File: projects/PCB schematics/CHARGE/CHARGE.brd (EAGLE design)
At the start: 160 x 100 mm, 42 parts, among them IC2 78L08SMD, Q1 IRLZ44Z, Q2 IRLZ44Z, Q3 IRLZ44Z, Q4 IRLZ44Z

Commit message: TSMPC - Initial draft (WIP).
Non-working commit of TSMPC.
Done simply to show possible board layout.
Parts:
- moved C9 435.3 mm to (96.5, 38.1)
- moved C11 431.1 mm to (106.7, 25.4)
- moved C10 430.7 mm to (99.1, 25.4)
- moved C8 430.4 mm to (91.4, 25.4)
- moved R10 428.1 mm to (82.5, 10.2)
- moved C7 426.7 mm to (106.7, 30.5)
- moved AND1 419.9 mm to (49.5, 3.81), turned to 90 degrees
- moved R14 417.9 mm to (64.8, 5.08), turned to 270 degrees
- moved OK1 415.6 mm to (74.9, 7.62), turned to 270 degrees
- moved C6 402.9 mm to (102.9, 11.4), turned to 90 degrees
- moved IC2 396.3 mm to (90.2, 16.5), turned to 90 degrees
- moved HV-OPA 375.6 mm to (90.2, 7.62), turned to 90 degrees
- moved R11 335.4 mm to (61.0, 17.8), turned to 90 degrees
- moved R13 324.7 mm to (58.4, 8.89)
- moved Q4 324.0 mm to (71.1, 27.9), turned to 270 degrees
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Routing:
- net AIR_CONTROL_SIGNAL: track 0.00 -> 109.9 mm, vias 0 -> 1
- net N$18: track 0.00 -> 99.0 mm, vias 0 -> 1
- net N$14: track 0.00 -> 88.2 mm
- net N$11: track 0.00 -> 84.9 mm
- net HV-: track 0.00 -> 81.7 mm
- net V+: track 0.00 -> 79.8 mm, vias 0 -> 2
- net N$24: track 0.00 -> 61.1 mm, vias 0 -> 1
- net HV+: track 0.00 -> 58.9 mm
- net VDIV_SIGNAL: track 0.00 -> 51.2 mm, vias 0 -> 2
- net +8V: track 0.00 -> 50.2 mm, vias 0 -> 4
- net HV-_CONTROL: track 0.00 -> 46.9 mm, vias 0 -> 1
- net N$9: track 0.00 -> 46.7 mm
- net N$3: track 0.00 -> 45.0 mm
- net N$7: track 0.00 -> 39.6 mm
- net VCC: track 0.00 -> 34.1 mm, vias 0 -> 2
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- added copper zone on layer 1, net GND
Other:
- board size 160 x 100 mm -> 111.7 x 86 mm

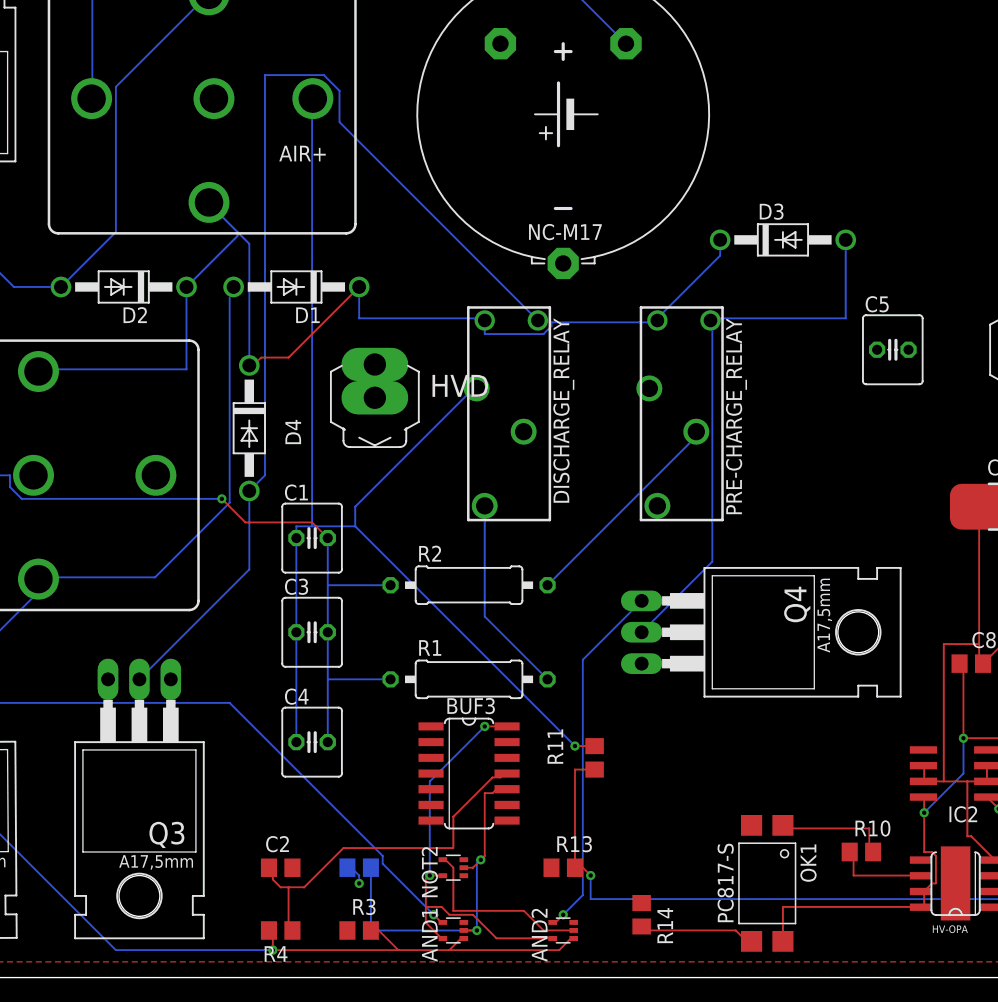
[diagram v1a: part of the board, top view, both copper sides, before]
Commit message: SC - Rev C; SC70 -> SOT23.
For single logic gate components, SC70 was initially chosen.
These packages proved too small to hand-solder.

All SC70 packages have been refactored to SOT23.

SparkFun DRC's added in for additional manufacturability.
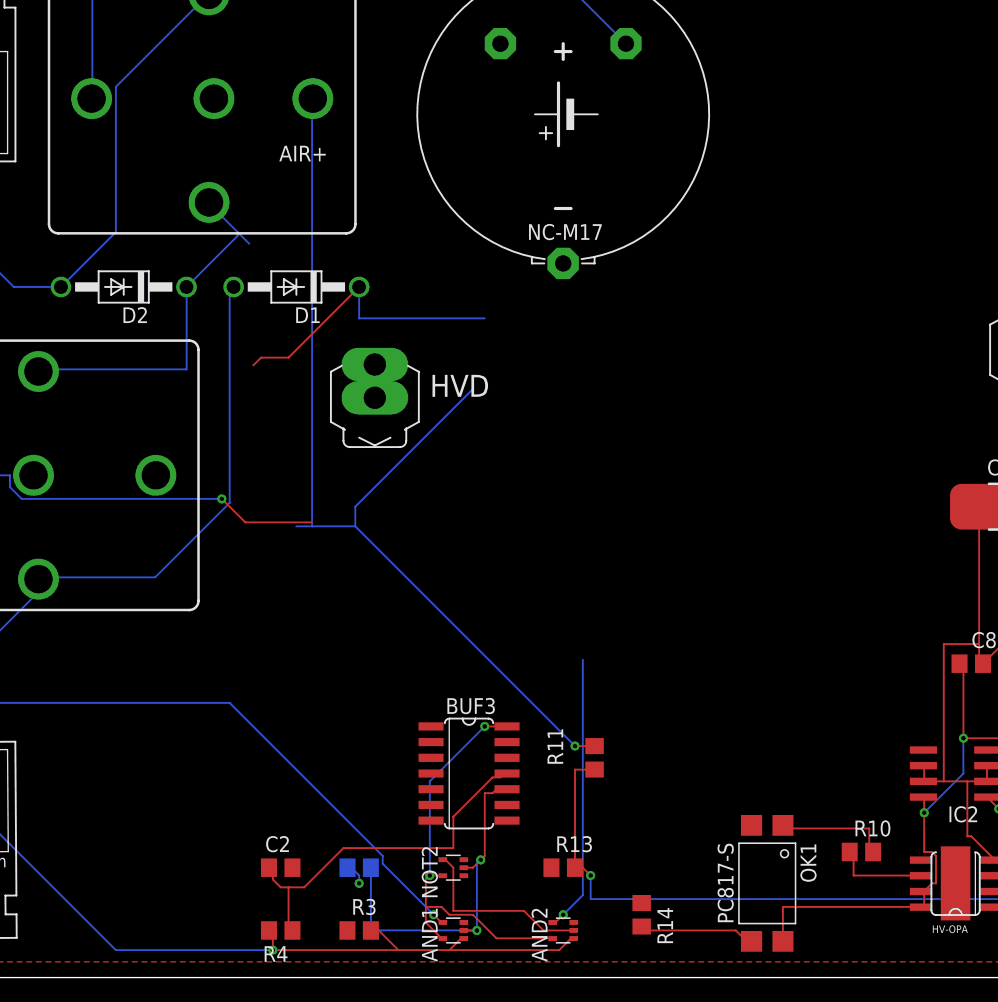
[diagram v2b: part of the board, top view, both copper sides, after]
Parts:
- removed C1, C3, C4, C5: (no value), rcl:C025-060X050
- removed D3, D4: 1N4933, diode:DO41-10
- removed DISCHARGE_RELAY, PRE-CHARGE_RELAY: CT112, relay:CT-SLIM
- removed Q3, Q4: IRLZ44Z, transistor-power:TO220BH
- removed R1, R2: (no value), rcl:0309/12
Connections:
- removed net N$1: PRE-CHARGE_RELAY.NO, R2.2
- removed net N$11: D4.A, DISCHARGE_RELAY.2, Q3.D
- removed net N$15: DISCHARGE_RELAY.NO
- removed net N$16: DISCHARGE_RELAY.C, R1.2
- removed net N$22: C5.2
- removed net N$23: C5.1
- removed net N$24: AIR-.87, C1.2, C3.2, C4.2, R1.1, R2.1
- removed net N$3: D3.A, PRE-CHARGE_RELAY.2, Q4.D
- removed net N$4: PRE-CHARGE_RELAY.NC
- new net N$27: AIR+.87
- new net N$31: AIR-.87
- net GND: no longer PRE-CHARGE_RELAY.C, Q3.S, Q4.S
- net N$14: no longer D3.C, D4.C, DISCHARGE_RELAY.1, PRE-CHARGE_RELAY.1
- net N$18: no longer AIR+.87, C1.1, C3.1, C4.1, DISCHARGE_RELAY.NC
- net N$2: no longer Q4.G
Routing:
- net N$11: track 84.9 -> 0.00 mm
- net N$24: track 61.1 -> 0.00 mm, vias 1 -> 0
- net N$3: track 45.0 -> 0.00 mm
- net N$14: track 88.2 -> 53.4 mm
- net N$31: track 0.00 -> 32.7 mm, vias 0 -> 1
- net N$18: track 99.0 -> 81.2 mm
- net N$1: track 17.5 -> 0.00 mm
- net N$16: track 16.1 -> 0.00 mm
- net N$2: track 29.1 -> 22.4 mm

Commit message: BSPD - Schematic revision/component revision.
During ESF, schematics chosen used European part libraries.
These were updated to US symbols, with appropriate final parts sourced
to allow builds of both SOP8 and DIL-8 packages.
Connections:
- new net N$1: HVD.1
- net N$14: no longer HVD.1
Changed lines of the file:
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@@
 </signal>
 <signal name="N$14">
-<contactref element="HVD" pad="1"/>
 <contactref element="AIR+" pad="86"/>
 <contactref element="D2" pad="C"/>
@@
 <wire x1="33.9725" y1="50.165" x2="36.195" y2="50.165" width="0.1524" layer="1"/>
 <wire x1="33.3375" y1="49.53" x2="33.9725" y2="50.165" width="0.1524" layer="1"/>
-<wire x1="41.91" y1="53.34" x2="43.18" y2="46.9138" width="0" layer="19" extent="16-16"/>
 <wire x1="27.94" y1="49.2125" x2="33.3375" y2="49.53" width="0" layer="19" extent="1-16"/>
 </signal>
@@
 <via x="30.7975" y="38.735" extent="1-16" drill="0.35"/>
 </signal>
+<signal name="N$1">
+<contactref element="HVD" pad="1"/>
+</signal>
 </signals>
